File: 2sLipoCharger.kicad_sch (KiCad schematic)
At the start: 32 parts, among them IC1 CN3702, J2 Conn_01x03_Pin, J6 Conn_01x01_Pin, Q2 PMOS, SW1 SW_SPDT

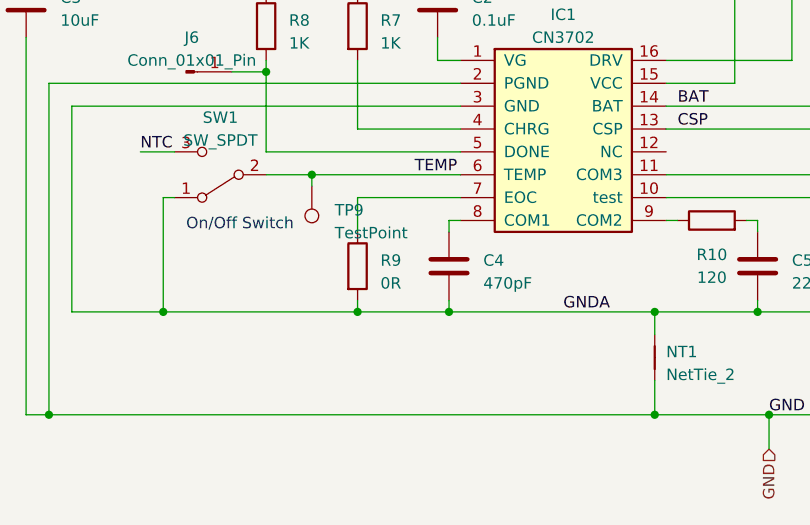
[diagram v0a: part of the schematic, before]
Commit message: Fixed problems after PCB fab
- SOT23 MOSFET footprint does not match part, needs to rotate (rerouting
  not done yet)

- EOC Resistor set to 100k
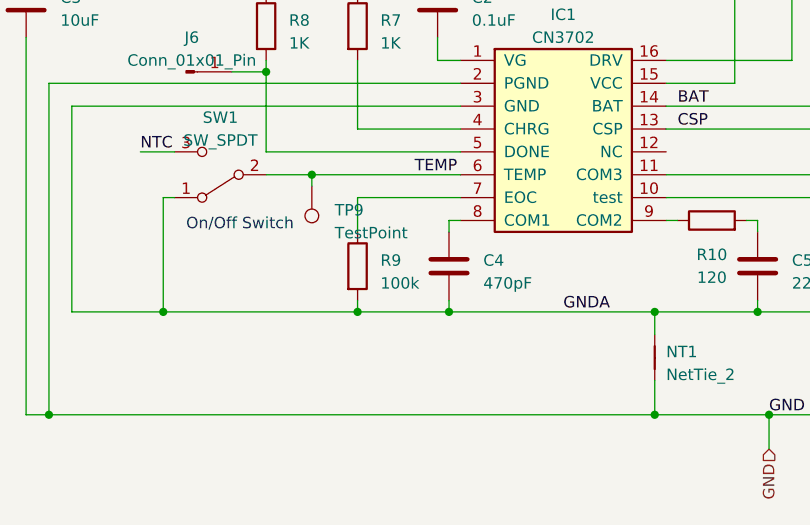
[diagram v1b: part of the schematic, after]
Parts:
- R9: value 0R -> 100k
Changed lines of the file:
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@@
       (effects (font (size 1.27 1.27)) (justify left))
     )
-    (property "Value" "0R" (at 127 117.475 0)
+    (property "Value" "100k" (at 127 117.475 0)
       (effects (font (size 1.27 1.27)) (justify left))
     )

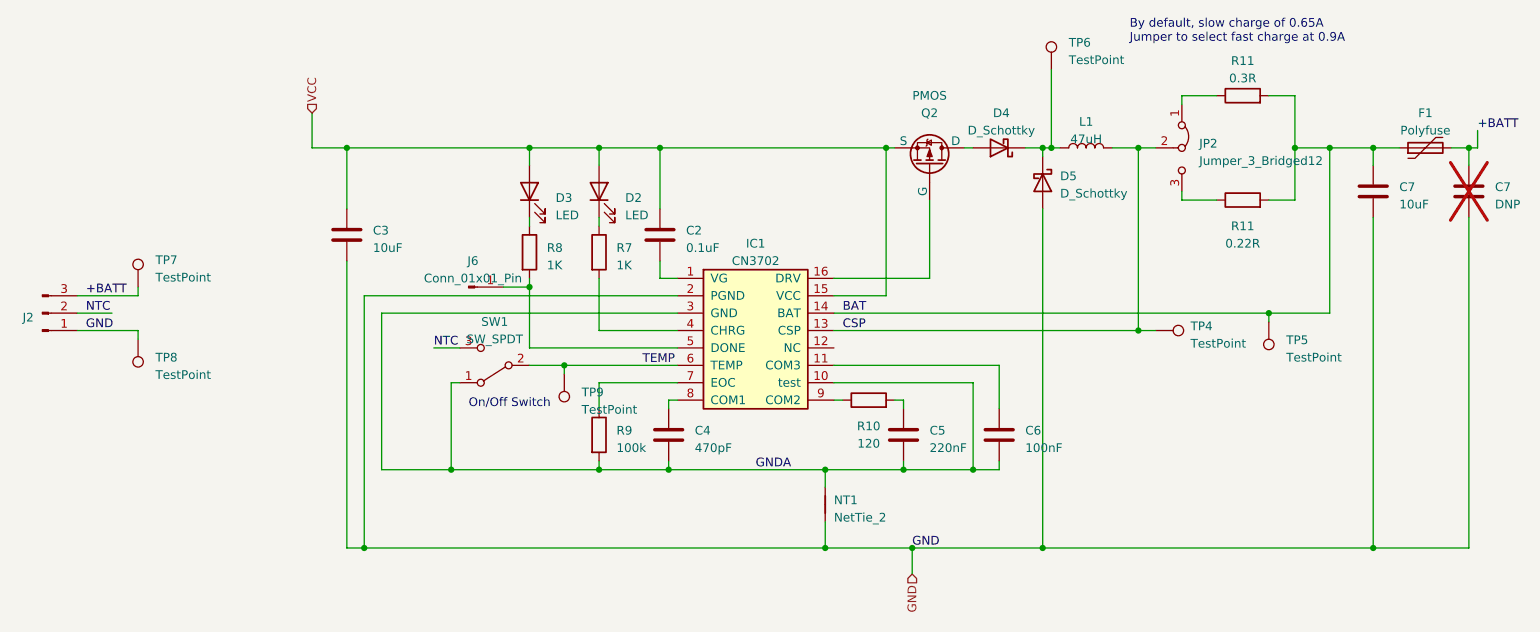
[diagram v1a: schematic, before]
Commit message: Fix the routing for rotated MOSFET
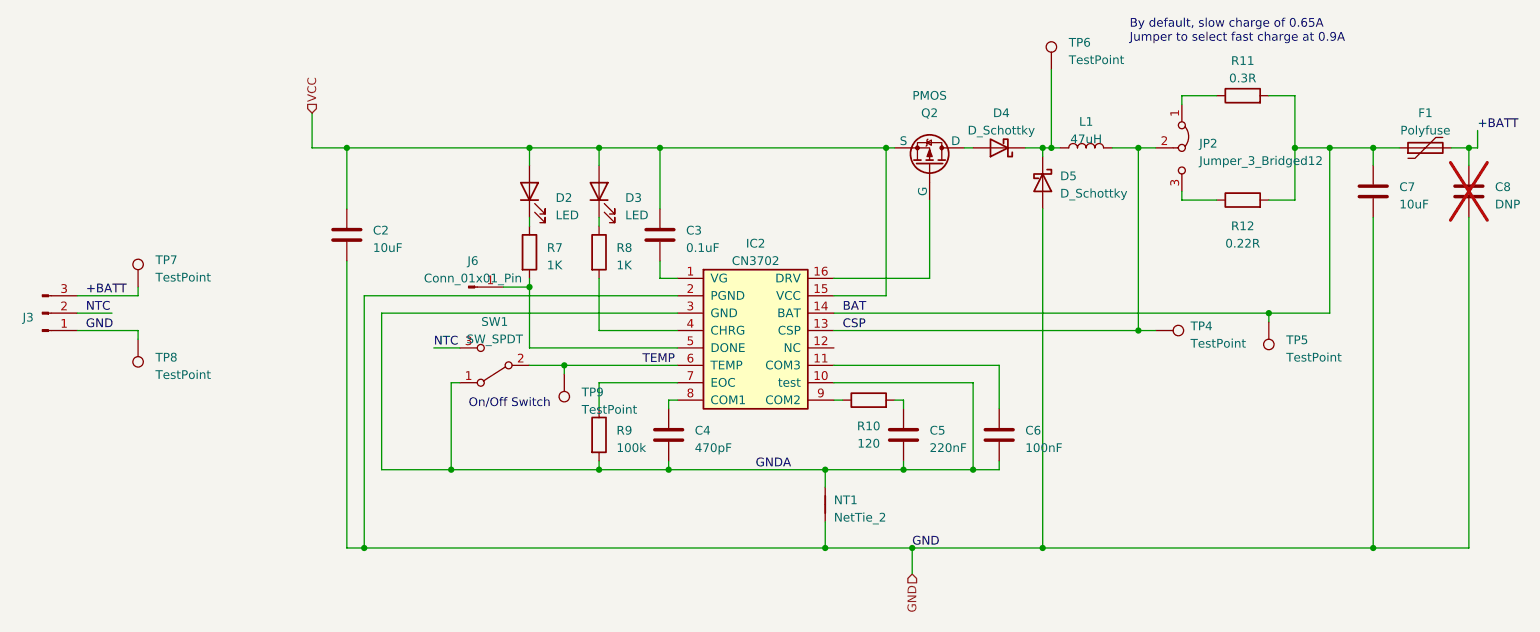
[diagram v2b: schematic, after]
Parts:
- renumbered C3 to C2, C2 to C3, C7 to C8, D3 to D2, D2 to D3, IC1 to IC2, J2 to J3, R11 to R12, R8 to R7, R7 to R8

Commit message: update JLCPCB part for R9,15,21
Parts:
- R9: JLCPCB Part # (none) -> C25803
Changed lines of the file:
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@@
+			)
+		)
+		(property "JLCPCB Part #" "C25803"
+			(at 124.46 115.57 0)
+			(effects
+				(font
+					(size 1.27 1.27)
+				)
+				(hide yes)
 			)
 		)
